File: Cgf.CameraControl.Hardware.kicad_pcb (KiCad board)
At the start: 2 copper layers, 26.5 x 55.5 mm, 27 parts, among them J1 5V input, J3 Pan, J4 Tilt, J5 SJ1-2503A, J6 Prog, J7 Sensor, Q1 BSS123, Q2 BSS123, Q4 MUN5211DW1, Q5 BSS123, U1 WT32-ETH01, U2 DRV8212DRLR, U3 DRV8212DRLR

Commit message: update schematic with suggestions
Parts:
- removed Q1: BSS123, Package_TO_SOT_SMD:SOT-23
- removed R1: 10K, Resistor_SMD:R_1206_3216Metric
- removed R2: 3.3K, Resistor_SMD:R_1206_3216Metric
- added R4: 150, Resistor_SMD:R_0805_2012Metric, B.Cu at (99.1, 59.3)
- added R6: 100, Resistor_SMD:R_0805_2012Metric, B.Cu at (99.1, 65.2)
- added U4: DRV8212DRLR, FootprintLibrary:SOT6_DRV8212_TEX, B.Cu at (112.7, 72.1)
- added U5: TXS0101DCK, Package_TO_SOT_SMD:SOT-363_SC-70-6, B.Cu at (117.8, 70.0)
- C1, C2, C3, C4, C5, C6: footprint Capacitor_SMD:C_1206_3216Metric -> Capacitor_SMD:C_0805_2012Metric
- R3: value 82 -> 150; footprint Resistor_SMD:R_1206_3216Metric -> Resistor_SMD:R_0805_2012Metric
- R5: value 47 -> 100; footprint Resistor_SMD:R_1206_3216Metric -> Resistor_SMD:R_0805_2012Metric
- R7, R8: footprint Resistor_SMD:R_1206_3216Metric -> Resistor_SMD:R_0805_2012Metric
- U2: footprint Package_TO_SOT_SMD:SOT-563 -> FootprintLibrary:SOT6_DRV8212_TEX
- U3: value DRV8212DRLR -> TXS0102DCT; footprint Package_TO_SOT_SMD:SOT-563 -> Package_SO:SSOP-8_2.95x2.8mm_P0.65mm
- moved Q4 57.8 mm to (117.8, 66.1), turned to 180 degrees
- moved J1 53.5 mm to (117.6, 50.0), turned to 180 degrees
- moved Q5 51.8 mm to (117.5, 61.9), turned to 180 degrees
- moved J6 49.7 mm to (108.1, 57.2), turned to 180 degrees
- moved Q2 48.3 mm to (117.5, 57.2), turned to 180 degrees
- moved R7 47.4 mm to (99.1, 68.1), turned to 180 degrees
- moved R8 46.3 mm to (99.1, 71.1), turned to 180 degrees
- moved D2 38.9 mm to (97.4, 52.5)
- moved D1 38.3 mm to (97.4, 49.3)
- moved C6 36.6 mm to (103.5, 71.4), turned to 180 degrees
- moved C2 35.9 mm to (103.5, 59.4), turned to 180 degrees
- moved R5 34.2 mm to (99.1, 62.2)
- moved C1 33.0 mm to (103.5, 56.3), turned to 180 degrees
- moved J3 32.9 mm to (113.0, 50.0)
- moved C4 32.7 mm to (103.5, 65.4), turned to 180 degrees
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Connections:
- D2 pad 3: Net-(D1-Pad3) -> Net-(D2-Pad3)
- D2 pad 4: Net-(D1-Pad4) -> Net-(D2-Pad4)
- U1 pad 17: Net-(J7-Pin_3) -> Net-(U1-IO35/ADC1_CH7/INPUT_ONLY)
- U1 pad 22: Net-(J7-Pin_2) -> Net-(U1-IO39/ADC1_CH3/INPUT_ONLY)
- U2 pad 1: +5V -> /tilt forward
- U2 pad 2: Net-(J3-Pin_1) -> /tilt backward
- U2 pad 3: Net-(J3-Pin_2) -> GND
- U2 pad 4: GND -> Net-(J4-Pin_2)
- U2 pad 5: /pan backward -> +5V
- U2 pad 6: /pan forward -> Net-(J4-Pin_1)
- U3 pad 1: +5V -> Net-(J7-Pin_3)
- U3 pad 2: Net-(J4-Pin_1) -> GND
- U3 pad 3: Net-(J4-Pin_2) -> +3V3
- U3 pad 4: GND -> Net-(U1-IO35/ADC1_CH7/INPUT_ONLY)
- U3 pad 5: /tilt backward -> Net-(U1-IO39/ADC1_CH3/INPUT_ONLY)
- U3 pad 6: /tilt forward -> +3V3
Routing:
- net GND: track 120.4 -> 0.00 mm
- net +5V: track 81.4 -> 0.00 mm, vias 2 -> 0
- net +3V3: track 55.3 -> 0.00 mm
- net Net-(J7-Pin_3): track 48.0 -> 0.00 mm
- net Net-(Q4A-B1): track 40.7 -> 0.00 mm
- net /GREEN: track 32.4 -> 0.00 mm, vias 1 -> 0
- net /lanc i/o: track 30.6 -> 0.00 mm
- net Net-(J7-Pin_2): track 26.8 -> 0.00 mm
- net /RED: track 22.2 -> 0.00 mm
- net /pan forward: track 20.7 -> 0.00 mm
- net Net-(Q5-D): track 20.7 -> 0.00 mm
- net /Prog_RX: track 20.3 -> 0.00 mm
- net /Prog_TX: track 18.5 -> 0.00 mm
- net /pan backward: track 18.0 -> 0.00 mm
- net /IO0: track 16.8 -> 0.00 mm
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
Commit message: Apply suggestions from review
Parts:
- added Q1: BSS123, Package_TO_SOT_SMD:SOT-23, B.Cu at (105.0, 38.8)
- added R1: 10K, Resistor_SMD:R_0805_2012Metric, B.Cu at (100.3, 37.9)
- added R2: 3.3K, Resistor_SMD:R_0805_2012Metric, B.Cu at (100.3, 40.9)
- added U5: 74LVC2T45DC, Package_SO:VSSOP-8_2.3x2mm_P0.5mm, B.Cu at (104.5, 34.7)

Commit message: wip
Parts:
- removed U3: TXS0102DCT, Package_SO:SSOP-8_2.95x2.8mm_P0.65mm
- removed the U5 at (117.8, 70.0)
- removed the U5 at (104.5, 34.7)
- added U5: 74LVC2T45DC, Package_SO:VSSOP-8_2.3x2mm_P0.5mm, B.Cu at (78.9, 31.2)
- moved J1 58.5 mm to (65.6, 23.4), turned to -90 degrees
- moved C6 58.3 mm to (66.7, 26.2), turned to 0 degrees
- moved J3 50.7 mm to (65.8, 68.5)
- moved Q4 50.0 mm to (86.7, 27.0), turned to 90 degrees
- moved Q2 48.8 mm to (70.9, 71.7), turned to -90 degrees
- moved U4 47.3 mm to (66.1, 64.3)
- moved R7 40.9 mm to (83.4, 30.4)
- moved R8 40.4 mm to (85.5, 33.0), turned to 0 degrees
- moved J6 39.4 mm to (87.9, 23.4), turned to 90 degrees
- moved D1 38.4 mm to (68.9, 75.0), turned to 0 degrees
- moved C4 37.0 mm to (67.4, 57.5), turned to 90 degrees
- moved Q5 36.3 mm to (82.6, 71.8), turned to -90 degrees
- moved C1 36.2 mm to (67.4, 54.1), turned to -90 degrees
- moved R1 35.2 mm to (76.9, 64.2), turned to -90 degrees
- moved C5 35.1 mm to (68.7, 64.3), turned to -90 degrees
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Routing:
- net GND: track 0.00 -> 141.3 mm
- net +5V: track 0.00 -> 99.7 mm, vias 0 -> 2
- net +3V3: track 0.00 -> 55.0 mm, vias 0 -> 1
- net /pan backward: track 0.00 -> 39.6 mm
- net /pan forward: track 0.00 -> 39.0 mm
- net /RED: track 0.00 -> 38.9 mm, vias 0 -> 1
- net /EN: track 0.00 -> 29.7 mm
- net /GREEN: track 0.00 -> 27.5 mm, vias 0 -> 1
- net Net-(U1-IO35/ADC1_CH7/INPUT_ONLY): track 0.00 -> 25.7 mm
- net /lanc i/o: track 0.00 -> 24.6 mm
- net Net-(Q2-D): track 0.00 -> 22.3 mm
- net /RTS: track 0.00 -> 20.2 mm, vias 0 -> 1
- net /IO0: track 0.00 -> 19.6 mm
- net Net-(Q5-D): track 0.00 -> 19.3 mm
- net Net-(J5-tip_front): track 0.00 -> 16.7 mm, vias 0 -> 1
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
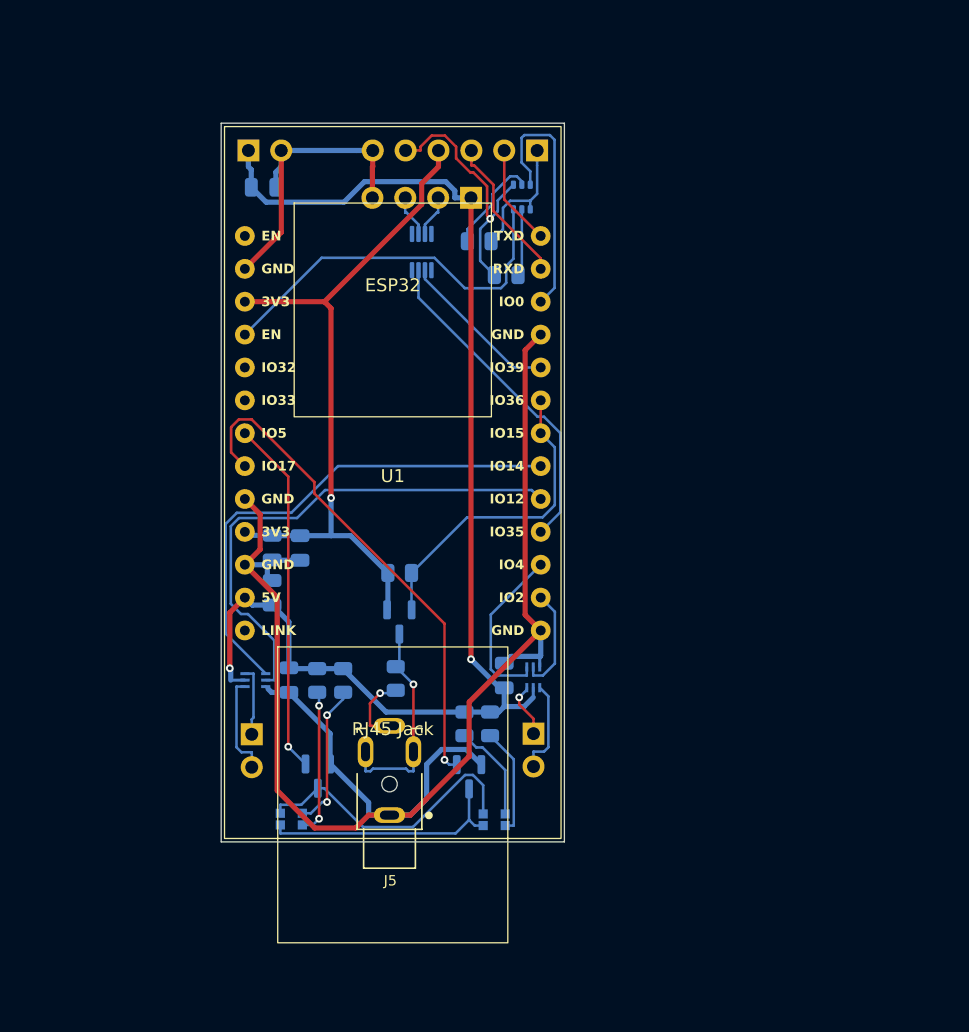
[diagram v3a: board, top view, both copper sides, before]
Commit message: Initial pcb layout
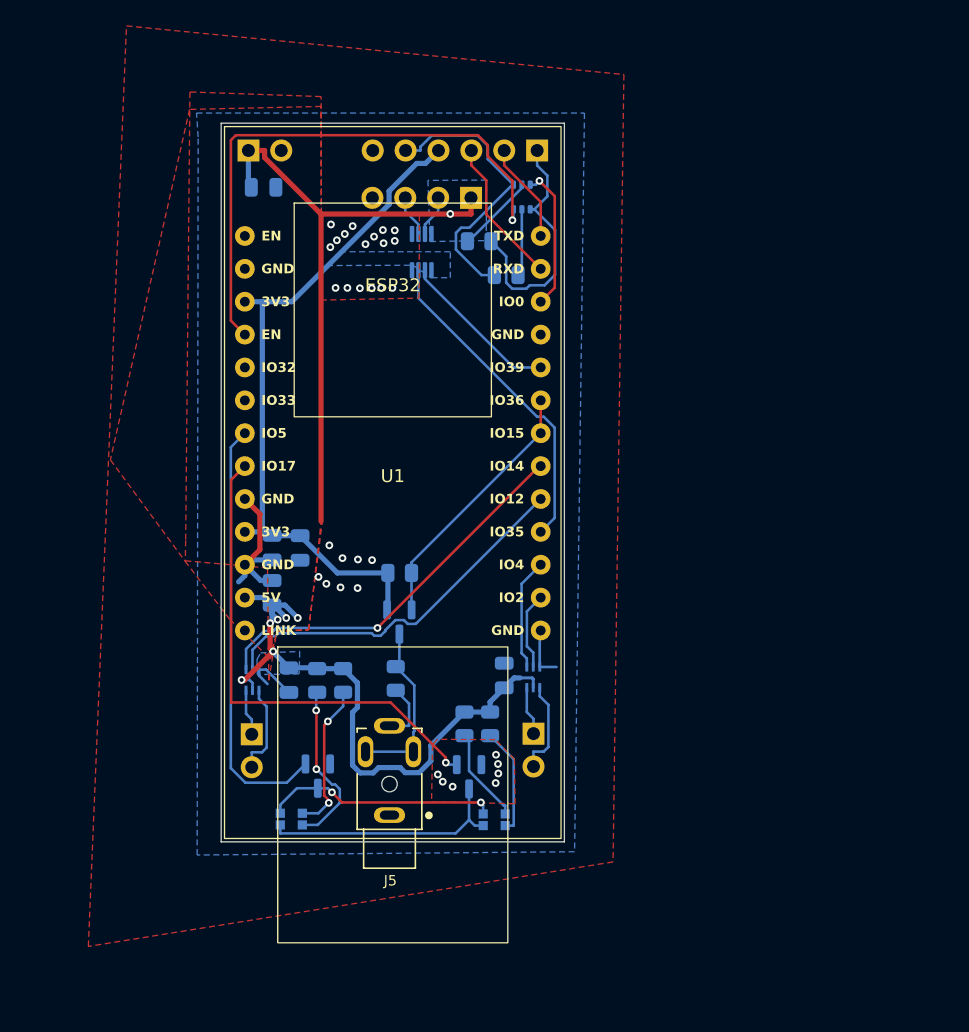
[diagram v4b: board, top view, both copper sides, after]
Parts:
- moved U4 0.22 mm to (65.9, 64.3), turned to -90 degrees
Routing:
- net GND: track 141.3 -> 21.0 mm, vias 0 -> 32
- net /EN: track 29.7 -> 43.3 mm, vias 0 -> 1
- net /pan backward: track 39.6 -> 29.1 mm
- net /DTR: track 10.1 -> 19.4 mm
- net /pan forward: track 39.0 -> 30.2 mm, vias 0 -> 1
- net /IO0: track 19.6 -> 11.1 mm, vias 0 -> 1
- net /GREEN: track 27.5 -> 33.2 mm, vias 1 -> 0
- net /tilt forward: track 13.3 -> 8.68 mm
- net /lanc i/o: track 24.6 -> 20.3 mm
- net Net-(Q2-D): track 22.3 -> 18.1 mm, vias 0 -> 2
- net Net-(J5-tip_front): track 16.7 -> 13.5 mm, vias 1 -> 0
- net +5V: track 99.7 -> 97.3 mm, vias 2 -> 7
- net /tilt backward: track 8.26 -> 6.01 mm
- net /RTS: track 20.2 -> 22.2 mm, vias 1 -> 0
- net Net-(J3-Pin_1): track 5.40 -> 3.58 mm
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- added copper zone on B.Cu, net +3V3
- added copper zone on B.Cu, net +5V
- added copper zone on F.Cu, net +5V
- added copper zone on B.Cu, net GND
- added copper zone on F.Cu, net GND

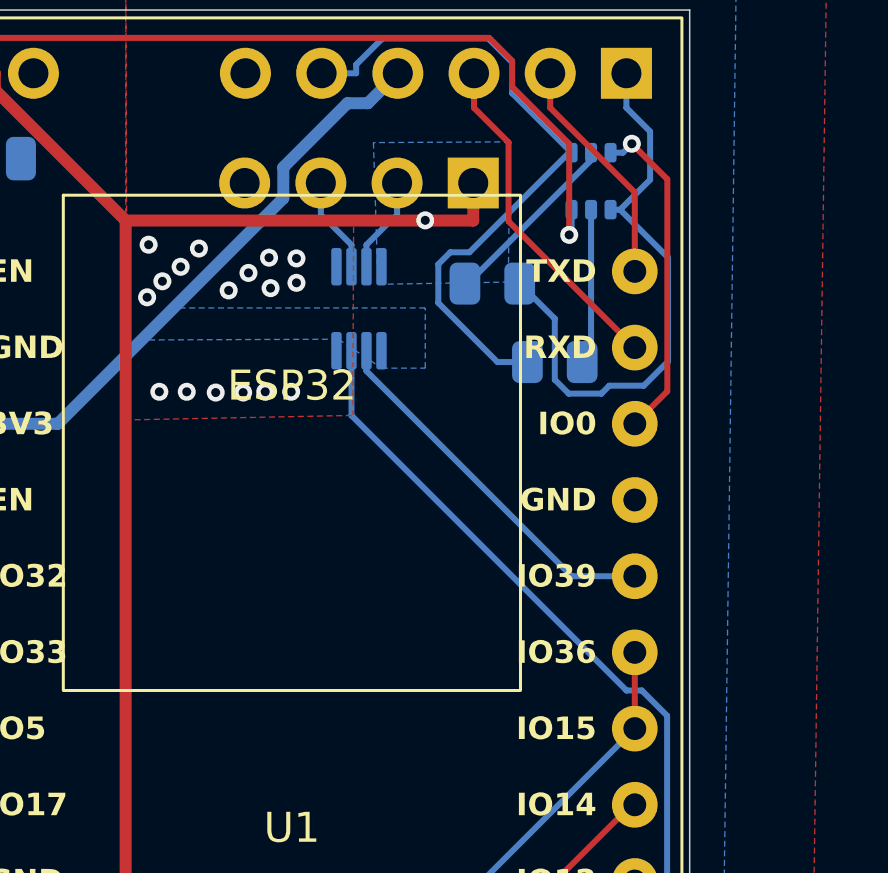
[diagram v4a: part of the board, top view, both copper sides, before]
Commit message: replace footprint after the pcb failed validation
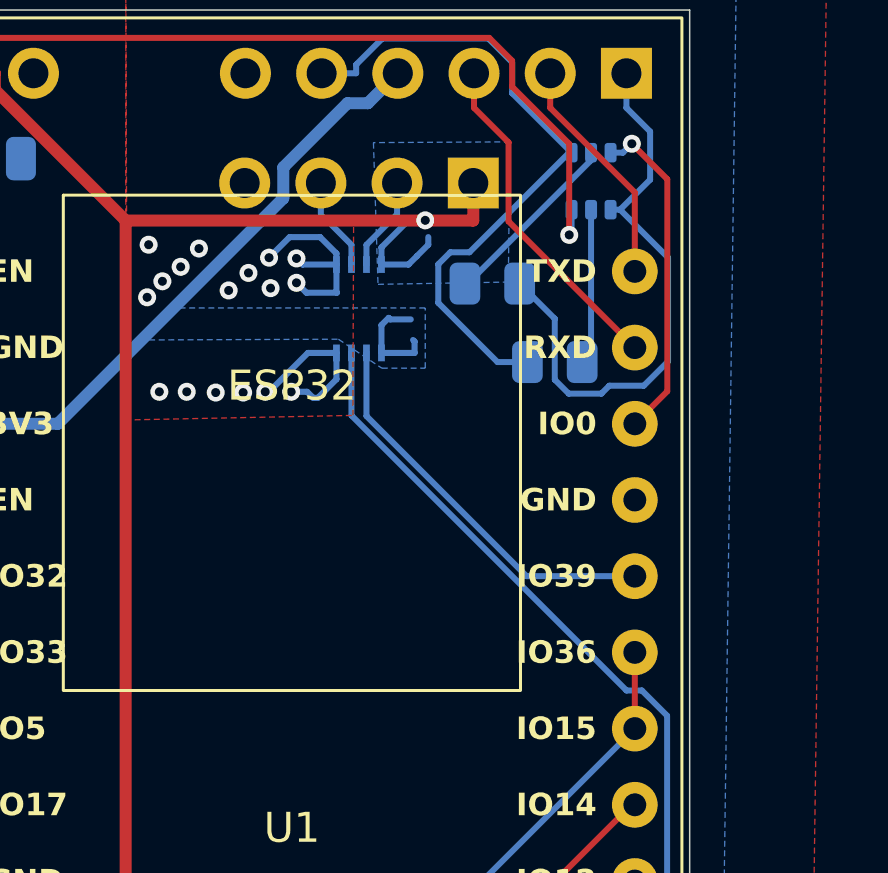
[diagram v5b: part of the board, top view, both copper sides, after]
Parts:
- U5: footprint Package_SO:VSSOP-8_2.3x2mm_P0.5mm -> FootprintLibrary:VSSOP8_74LVC2T45DC_125_NEX-L
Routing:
- net GND: track 21.0 -> 33.6 mm
- net +5V: track 97.3 -> 101.8 mm
- net +3V3: track 53.4 -> 57.0 mm
- net Net-(U1-IO39/ADC1_CH3/INPUT_ONLY): track 12.5 -> 13.3 mm

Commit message: improve layout
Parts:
- moved R3 2.04 mm to (70.7, 66.3)
- moved R5 2.03 mm to (72.8, 66.3)
- moved C5 0.10 mm to (68.6, 64.3), turned to 90 degrees
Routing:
- net GND: track 33.6 -> 160.0 mm, vias 32 -> 133
- net +5V: track 101.8 -> 125.7 mm, vias 7 -> 3
- net Net-(Q5-D): track 19.3 -> 41.2 mm
- net +3V3: track 57.0 -> 75.1 mm
- net /EN: track 43.3 -> 30.0 mm, vias 1 -> 2
- net /DTR: track 19.4 -> 10.4 mm
- net /pan forward: track 30.2 -> 38.5 mm
- net /IO0: track 11.1 -> 19.3 mm, vias 1 -> 0
- net Net-(U1-IO35/ADC1_CH7/INPUT_ONLY): track 25.2 -> 30.7 mm
- net /GREEN: track 33.2 -> 27.8 mm, vias 0 -> 2
- net Net-(D1-Pad4): track 13.1 -> 9.33 mm
- net /RTS: track 22.2 -> 19.4 mm
- net Net-(U1-IO39/ADC1_CH3/INPUT_ONLY): track 13.3 -> 16.0 mm
- net Net-(D1-Pad3): track 11.7 -> 9.52 mm
- net Net-(Q4B-B2): track 5.20 -> 7.29 mm
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- removed copper zone on B.Cu, net +3V3
- removed copper zone on B.Cu, net +5V
- removed copper zone on F.Cu, net +5V

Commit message: Fix all design rules
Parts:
- J5: moved to B.Cu
- moved R5 0.38 mm to (72.9, 66.0)
- turned J5 to 0 degrees
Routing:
- net Net-(Q5-D): track 41.2 -> 28.6 mm, vias 0 -> 2
- net Net-(U1-IO35/ADC1_CH7/INPUT_ONLY): track 30.7 -> 27.9 mm, vias 0 -> 2

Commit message: improve pcb
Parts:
- moved C5 3.41 mm to (65.2, 64.2)
- moved U4 1.40 mm to (67.3, 64.2)
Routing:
- net +5V: track 125.7 -> 98.4 mm, vias 3 -> 1
- net GND: track 160.0 -> 143.8 mm, vias 133 -> 210
- net +3V3: track 75.1 -> 65.9 mm, vias 0 -> 1
- net /IO0: track 19.3 -> 10.2 mm
- net Net-(Q5-D): track 28.6 -> 37.5 mm, vias 2 -> 0
- net /pan forward: track 38.5 -> 29.7 mm, vias 1 -> 0
- net /EN: track 30.0 -> 36.4 mm, vias 2 -> 0
- net /RED: track 38.3 -> 33.8 mm
- net Net-(U1-IO35/ADC1_CH7/INPUT_ONLY): track 27.9 -> 24.1 mm, vias 2 -> 1
- net /DTR: track 10.4 -> 14.1 mm, vias 0 -> 2
- net Net-(U1-IO39/ADC1_CH3/INPUT_ONLY): track 15.8 -> 12.3 mm, vias 0 -> 1
- net Net-(J5-tip_front): track 15.0 -> 17.7 mm, vias 0 -> 1
- net Net-(Q4B-B2): track 7.29 -> 5.20 mm
- net Net-(J3-Pin_2): track 6.67 -> 8.61 mm, vias 0 -> 1
- net /GREEN: track 27.8 -> 28.9 mm, vias 2 -> 0
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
